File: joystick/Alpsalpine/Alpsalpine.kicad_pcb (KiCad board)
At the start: 2 copper layers, 1 part

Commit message: update joystick label to global
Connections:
- net /ADC0 renamed ADC1
- net /ADC1 renamed ADC0
- net /GND renamed GND
- net /JT_B2 renamed JT_B2
- net /VCC renamed VCC
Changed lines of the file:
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@@
 	)
 	(net 0 "")
-	(net 1 "/ADC0")
-	(net 2 "/GND")
-	(net 3 "/ADC1")
-	(net 4 "/VCC")
-	(net 5 "/JT_B2")
+	(net 1 "JT_B2")
+	(net 2 "ADC0")
+	(net 3 "VCC")
+	(net 4 "ADC1")
+	(net 5 "GND")
 	(footprint "ErgoCai.pretty:Alpsalpine_RKJXV122400R"
 		(layer "F.Cu")
@@
 			(layers "*.Cu" "*.Mask")
 			(remove_unused_layers no)
-			(net 2 "/GND")
+			(net 5 "GND")
 			(pinfunction "GND0")
 			(pintype "input")
@@
 			(layers "*.Cu" "*.Mask")
 			(remove_unused_layers no)
-			(net 3 "/ADC1")
+			(net 2 "ADC0")
 			(pinfunction "ADC0")
 			(pintype "output")
@@
 			(layers "*.Cu" "*.Mask")
 			(remove_unused_layers no)
-			(net 4 "/VCC")
+			(net 3 "VCC")
 			(pinfunction "VCC0")
 			(pintype "input")
@@
 			(layers "*.Cu" "*.Mask")
 			(remove_unused_layers no)
-			(net 2 "/GND")
+			(net 5 "GND")
 			(pinfunction "GND1")
 			(pintype "input")
@@
 			(layers "*.Cu" "*.Mask")
 			(remove_unused_layers no)
-			(net 1 "/ADC0")
+			(net 4 "ADC1")
 			(pinfunction "ADC1")
 			(pintype "output")
@@
 			(layers "*.Cu" "*.Mask")
 			(remove_unused_layers no)
-			(net 4 "/VCC")
+			(net 3 "VCC")
 			(pinfunction "VCC1")
 			(pintype "input")
@@
 			(layers "*.Cu" "*.Mask")
 			(remove_unused_layers no)
-			(net 2 "/GND")
+			(net 5 "GND")
 			(pinfunction "A")
 			(pintype "input")
@@
 			(layers "*.Cu" "*.Mask")
 			(remove_unused_layers no)
-			(net 5 "/JT_B2")
+			(net 1 "JT_B2")
 			(pinfunction "B")
 			(pintype "input")
@@
 			(layers "*.Cu" "*.Mask")
 			(remove_unused_layers no)
-			(net 2 "/GND")
+			(net 5 "GND")
 			(pinfunction "C")
 			(pintype "input")
@@
 			(layers "*.Cu" "*.Mask")
 			(remove_unused_layers no)
-			(net 5 "/JT_B2")
+			(net 1 "JT_B2")
 			(pinfunction "D")
 			(pintype "input")
@@
 	)
 	(segment
+		(start -3.25 10.25)
+		(end 3.25 10.25)
+		(width 0.2)
+		(layer "F.Cu")
+		(net 1)
+	)
+	(segment
+		(start 8.73 -2.5)
+		(end 3.73 -2.5)
+		(width 0.2)
+		(layer "B.Cu")
+		(net 3)
+	)
+	(segment
+		(start 3.73 -2.5)
+		(end -2.5 -8.73)
+		(width 0.2)
+		(layer "B.Cu")
+		(net 3)
+	)
+	(segment
+		(start 8.73 2.5)
+		(end 2.5 -3.73)
+		(width 0.2)
+		(layer "F.Cu")
+		(net 5)
+	)
+	(segment
+		(start -3.25 5.75)
+		(end 3.25 5.75)
+		(width 0.2)
+		(layer "F.Cu")
+		(net 5)
+	)
+	(segment
 		(start 2.5 -3.73)
 		(end 2.5 -8.73)
 		(width 0.2)
 		(layer "F.Cu")
-		(net 2)
+		(net 5)
 	)
 	(segment
@@
 		(width 0.2)
 		(layer "F.Cu")
-		(net 2)
+		(net 5)
 	)
 	(segment
@@
 		(width 0.2)
 		(layer "F.Cu")
-		(net 2)
-	)
-	(segment
-		(start 8.73 2.5)
-		(end 2.5 -3.73)
-		(width 0.2)
-		(layer "F.Cu")
-		(net 2)
-	)
-	(segment
-		(start -3.25 5.75)
-		(end 3.25 5.75)
-		(width 0.2)
-		(layer "F.Cu")
-		(net 2)
-	)
-	(segment
-		(start 3.73 -2.5)
-		(end -2.5 -8.73)
-		(width 0.2)
-		(layer "B.Cu")
-		(net 4)
-	)
-	(segment
-		(start 8.73 -2.5)
-		(end 3.73 -2.5)
-		(width 0.2)
-		(layer "B.Cu")
-		(net 4)
-	)
-	(segment
-		(start 3.25 10.25)
-		(end -3.25 10.25)
-		(width 0.2)
-		(layer "F.Cu")

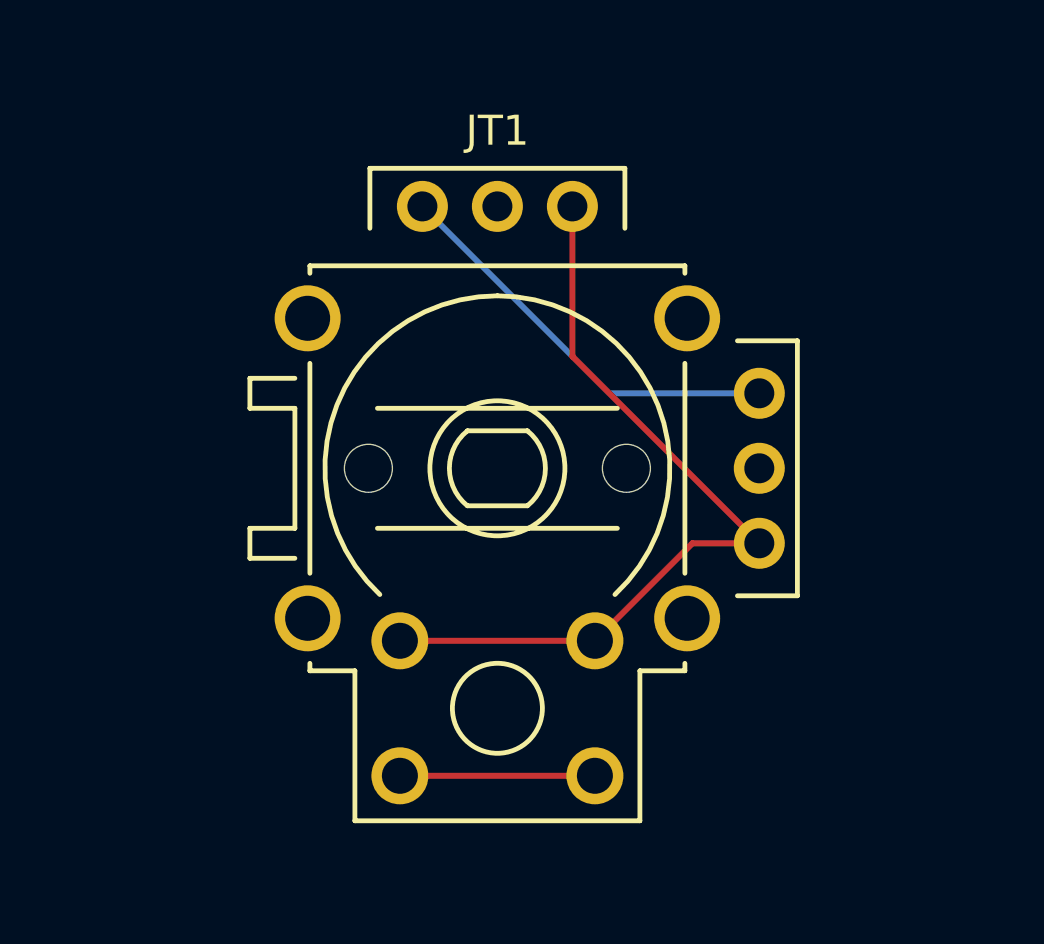
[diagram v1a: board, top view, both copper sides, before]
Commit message: add joystick module
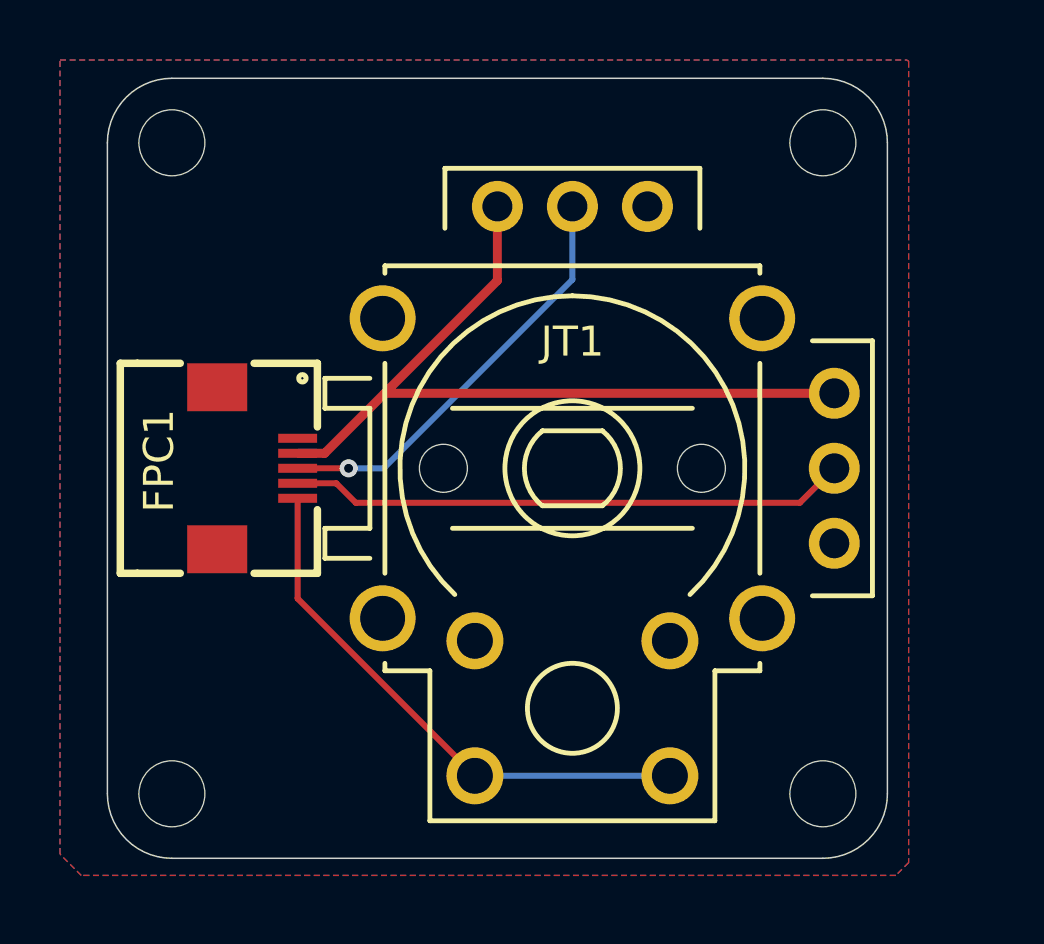
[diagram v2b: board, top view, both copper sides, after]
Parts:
- added FPC1: AFC01-S05FCA-00, ErgoCai.pretty:FPC-SMD_AFC01-S05FCA-00, F.Cu at (-8.00, 0.00)
- added H1: MountingHole, MountingHole:MountingHole_2.2mm_M2_DIN965, F.Cu at (-10.8, -10.8)
- added H2: MountingHole, MountingHole:MountingHole_2.2mm_M2_DIN965, F.Cu at (10.8, -10.8)
- added H3: MountingHole, MountingHole:MountingHole_2.2mm_M2_DIN965, F.Cu at (-10.8, 10.8)
- added H4: MountingHole, MountingHole:MountingHole_2.2mm_M2_DIN965, F.Cu at (10.8, 10.8)
- moved JT1 2.50 mm to (2.50, 0.00)
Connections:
- net JT_B2 renamed JT_B1
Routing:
- net GND: track 27.1 -> 0.00 mm
- net ADC0: track 0.00 -> 18.6 mm
- net ADC1: track 0.00 -> 14.2 mm, vias 0 -> 1
- net VCC: track 13.8 -> 26.5 mm
- net JT_B1: track 6.50 -> 18.2 mm
- added copper zone on B.Cu, net GND
- added copper zone on F.Cu, net GND
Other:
- board outline added: 26 x 26 mm
- board text added: "GND"
- board text added: "SW"
- board text added: "VCC"
- board text added: "VRX"
- board text added: "VRY"

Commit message: add RGB WS2812B modules
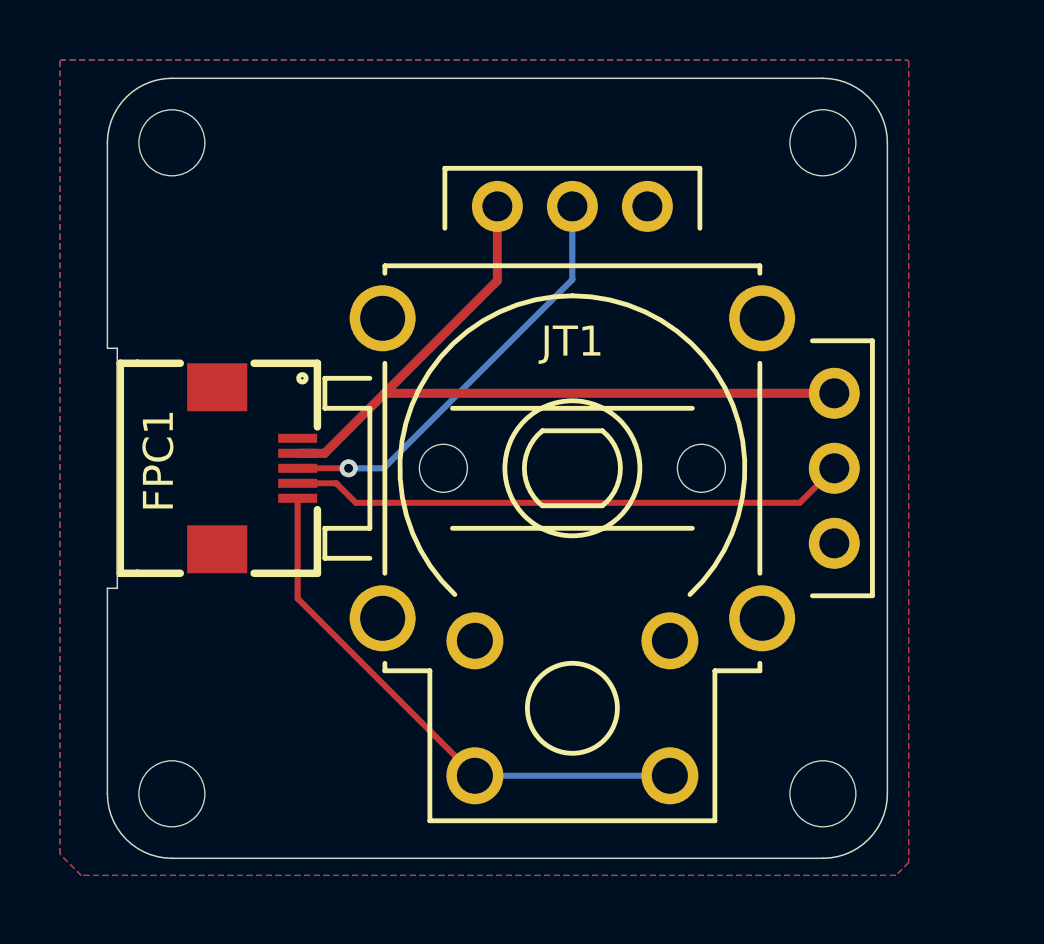
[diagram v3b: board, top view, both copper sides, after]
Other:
- outline, holes or cut-outs redrawn
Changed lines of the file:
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@@
+	)
+	(gr_line
+		(start -12.67 -4)
+		(end -12.67 4)
+		(stroke
+			(width 0.05)
+			(type solid)
+		)
+		(layer "Edge.Cuts")
 	)
 	(gr_line
@@
 		(layer "Edge.Cuts")
 	)
+	(gr_line
+		(start -12.99 -4)
+		(end -12.67 -4)
+		(stroke
+			(width 0.05)
+			(type solid)
+		)
+		(layer "Edge.Cuts")
+	)
 	(gr_arc
 		(start 13 10.85)
@@
 	)
 	(gr_line
-		(start -13 10.85)
-		(end -13 -10.85)
+		(start -12.67 4)
+		(end -13 4)
 		(stroke
 			(width 0.05)
 			(type solid)
+		)
+		(layer "Edge.Cuts")
+	)
+	(gr_line
+		(start -13 4)
+		(end -13 10.850001)
+		(stroke
+			(width 0.05)
+			(type default)
 		)
 		(layer "Edge.Cuts")
@@
 		)
 		(layer "Edge.Cuts")
+	)
+	(gr_line
+		(start -12.999999 -10.85)
+		(end -12.999999 -4)
+		(stroke
+			(width 0.05)
+			(type default)
+		)
+		(layer "Edge.Cuts")

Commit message: update joystick mount
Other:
- outline, holes or cut-outs redrawn
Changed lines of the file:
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@@
 		)
 		(embedded_fonts no)
-		(model "${EASYEDA2KICAD}/easyeda2kicad.3dshapes/FPC-SMD_AFC01-S05FCA-00.wrl"
-			(offset
-				(xyz 0 -1.32 -0)
-			)
-			(scale
-				(xyz 1 1 1)
-			)
-			(rotate
-				(xyz 0 0 0)
-			)
-		)
-		(model "/Users/jinsongc/Documents/KiCad/easyeda2kicad/easyeda2kicad.3dshapes/FPC-SMD_AFC01-S05FCA-00.step"
+		(model "/Users/jinsongc/Development/ErgoCaiLib/3dmodels/FPC-SMD_AFC01-S05FCA-00.step"
 			(offset
 				(xyz 0 -1 2)
@@
 	)
 	(gr_line
-		(start -12.67 -4)
-		(end -12.67 4)
-		(stroke
-			(width 0.05)
-			(type solid)
-		)
-		(layer "Edge.Cuts")
-	)
-	(gr_line
 		(start 13 10.85)
 		(end 13 -10.85)
@@
 		(layer "Edge.Cuts")
 	)
-	(gr_line
-		(start -12.99 -4)
-		(end -12.67 -4)
-		(stroke
-			(width 0.05)
-			(type solid)
-		)
-		(layer "Edge.Cuts")
-	)
 	(gr_arc
 		(start 13 10.85)
 		(mid 12.37028 12.37028)
 		(end 10.85 13)
-		(stroke
-			(width 0.05)
-			(type solid)
-		)
-		(layer "Edge.Cuts")
-	)
-	(gr_line
-		(start -12.67 4)
-		(end -13 4)
 		(stroke
 			(width 0.05)
@@
 	(gr_line
 		(start -12.999999 -10.85)
-		(end -12.999999 -4)
+		(end -12.999999 4)
 		(stroke
 			(width 0.05)

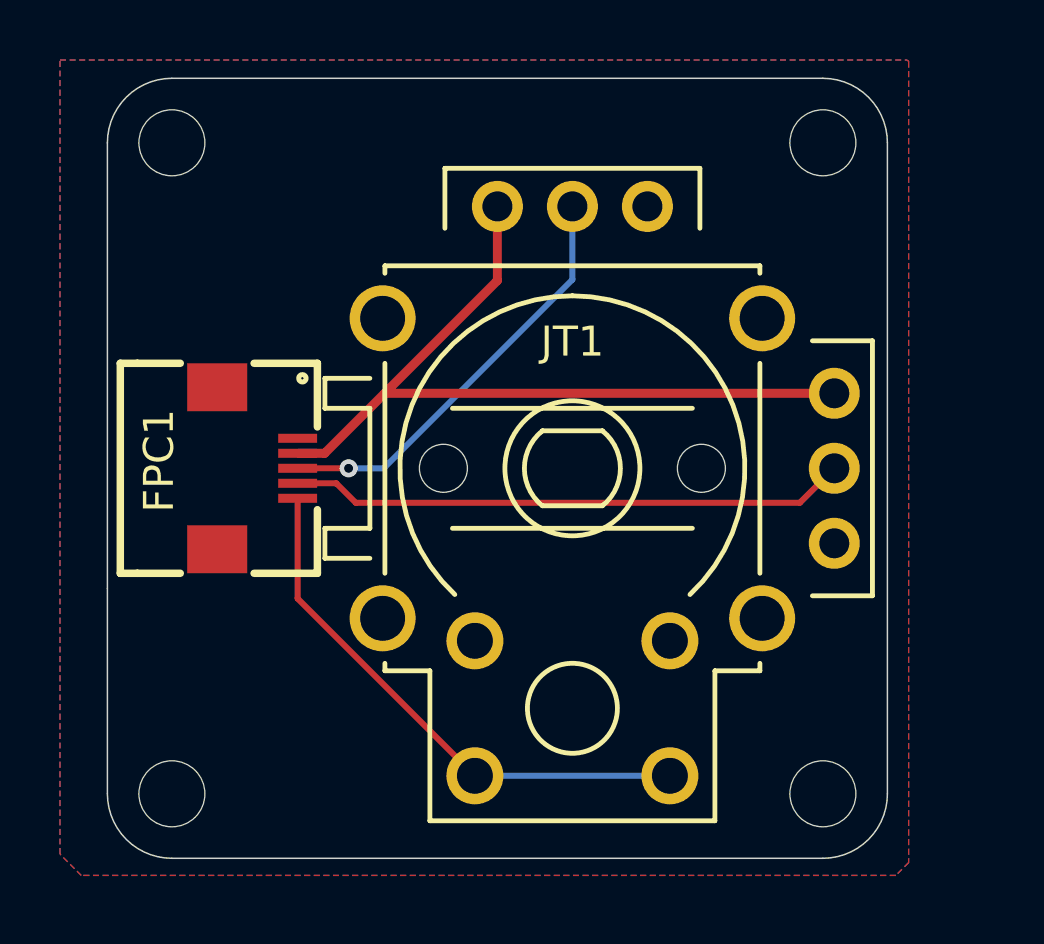
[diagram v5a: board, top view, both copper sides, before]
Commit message: update joystick size
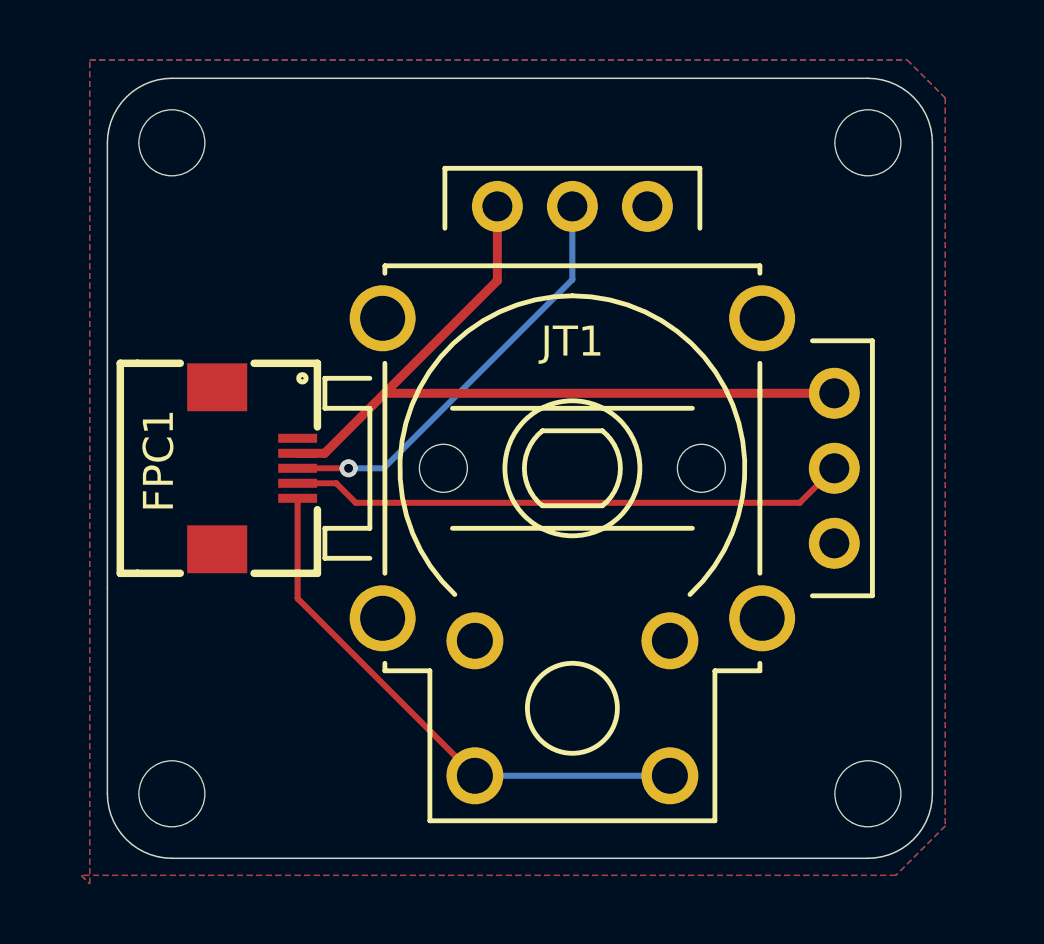
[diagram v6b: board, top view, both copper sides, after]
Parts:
- moved H2 1.50 mm to (12.3, -10.8)
- moved H4 1.50 mm to (12.3, 10.8)
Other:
- board size 26 x 26 mm -> 27.5 x 26 mm
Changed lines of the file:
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@@
 	(footprint "MountingHole:MountingHole_2.2mm_M2_DIN965"
 		(layer "F.Cu")
-		(at 10.85 -10.85)
+		(at 12.35 -10.85)
 		(descr "Mounting Hole 2.2mm, M2, no annular, generated by kicad-footprint-generator mountinghole.py")
 		(tags "mountinghole M2 DIN965")
@@
 	(footprint "MountingHole:MountingHole_2.2mm_M2_DIN965"
 		(layer "F.Cu")
-		(at 10.85 10.85)
+		(at 12.35 10.85)
 		(descr "Mounting Hole 2.2mm, M2, no annular, generated by kicad-footprint-generator mountinghole.py")
 		(tags "mountinghole M2 DIN965")
@@
 			)
 		)
-		(model "/Users/jinsongc/Desktop/Alpsalpine.step"
+		(model "/Users/jinsongc/Development/ErgoCaiLib/3dmodels/Joystick Cap.stp"
+			(opacity 0.7800)
 			(offset
 				(xyz 0 0 18)
@@
 			)
 			(rotate
-				(xyz -0 -0 -0)
+				(xyz -0 180 180)
 			)
 		)
@@
 	)
 	(gr_line
-		(start 13 10.85)
-		(end 13 -10.85)
+		(start 14.5 10.85)
+		(end 14.5 -10.85)
 		(stroke
 			(width 0.05)
@@
 	)
 	(gr_arc
-		(start 10.85 -13)
-		(mid 12.37028 -12.37028)
-		(end 13 -10.85)
+		(start 12.35 -13)
+		(mid 13.87028 -12.37028)
+		(end 14.5 -10.85)
 		(stroke
 			(width 0.05)
@@
 	)
 	(gr_arc
-		(start 13 10.85)
-		(mid 12.37028 12.37028)
-		(end 10.85 13)
+		(start 14.5 10.85)
+		(mid 13.87028 12.37028)
+		(end 12.35 13)
 		(stroke
 			(width 0.05)
@@
 	(gr_line
 		(start -10.85 13)
-		(end 10.85 13)
+		(end 12.35 13)
 		(stroke
 			(width 0.05)
@@
 	)
 	(gr_line
-		(start 10.85 -13)
+		(start 12.35 -13)
 		(end -10.85 -13)
 		(stroke
@@
 		(polygon
 			(pts
-				(xy -14.58 -13.61) (xy 13.66 -13.61) (xy 13.71 -13.56) (xy 13.71 13.14) (xy 13.28 13.57) (xy -13.87 13.57)
-				(xy -14.58 12.86)
-			)
-		)
+				(xy -13.59 -13.61) (xy 13.66 -13.61) (xy 14.93 -12.34) (xy 14.93 11.92) (xy 13.28 13.57) (xy -13.87 13.57)
+				(xy -13.59 13.85)
+			)
+		)

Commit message: add RGB led in e-paper module
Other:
- outline, holes or cut-outs redrawn
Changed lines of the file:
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@@
+		(layer "Edge.Cuts")
+	)
+	(gr_line
+		(start -13 -10.85)
+		(end -13 -4)
+		(stroke
+			(width 0.05)
+			(type solid)
+		)
 		(layer "Edge.Cuts")
 	)
@@
 	)
 	(gr_line
-		(start -13 4)
-		(end -13 10.850001)
+		(start -12.5 4)
+		(end -13 4)
 		(stroke
 			(width 0.05)
-			(type default)
+			(type solid)
+		)
+		(layer "Edge.Cuts")
+	)
+	(gr_line
+		(start -13 4)
+		(end -13 10.85)
+		(stroke
+			(width 0.05)
+			(type solid)
 		)
 		(layer "Edge.Cuts")
@@
 	)
 	(gr_line
-		(start -12.999999 -10.85)
-		(end -12.999999 4)
+		(start -12.5 -4)
+		(end -12.5 4)
 		(stroke
 			(width 0.05)
-			(type default)
+			(type solid)
 		)
 		(layer "Edge.Cuts")
@@
 		(stroke
 			(width 0.05)
+			(type solid)
+		)
+		(layer "Edge.Cuts")
+	)
+	(gr_line
+		(start -13 -4)
+		(end -12.5 -4)
+		(stroke
+			(width 0.05)

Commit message: update joystick FPC to 6 pins
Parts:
- removed FPC1: AFC01-S05FCA-00, ErgoCai.pretty:FPC-SMD_AFC01-S05FCA-00
- added JT_J2: AFD01-S06FCA-00, ErgoCai.pretty:FPC-SMD_6P-P0.50_JS_AFD01-S06FCA-00, F.Cu at (9.78, 0.00)
- moved JT_J1 2.50 mm to (0.00, 0.00), turned to 180 degrees
- renumbered JT1 to JT_J1
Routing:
- net GND: track 0.00 -> 38.1 mm
- net VCC: track 26.5 -> 29.5 mm, vias 0 -> 1
- net JT_B1: track 18.2 -> 20.9 mm
- net ADC1: track 14.2 -> 12.5 mm, vias 1 -> 0
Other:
- outline, holes or cut-outs redrawn
